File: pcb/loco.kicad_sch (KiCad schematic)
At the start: 121 parts, among them J1 I2C, J10 Stepper1, J11 Motor2, J12 PWR1, J13 PWR2, J14 Stepper1, J15 Stepper1, J2 EXT, J3 GPIO, J6 USB_C_Receptacle_USB2.0, J7 UART, J8 TagConnect, J9 Motor1, U1 LD1117S33TR_SOT223, U2 STM32C031CxUx, U3 STSPIN240, U4 STSPIN220, U5 AP22652_3x, U6 AP22652_3x, U7 AP22652_3x, U8 STSPIN220, U9 STSPIN220

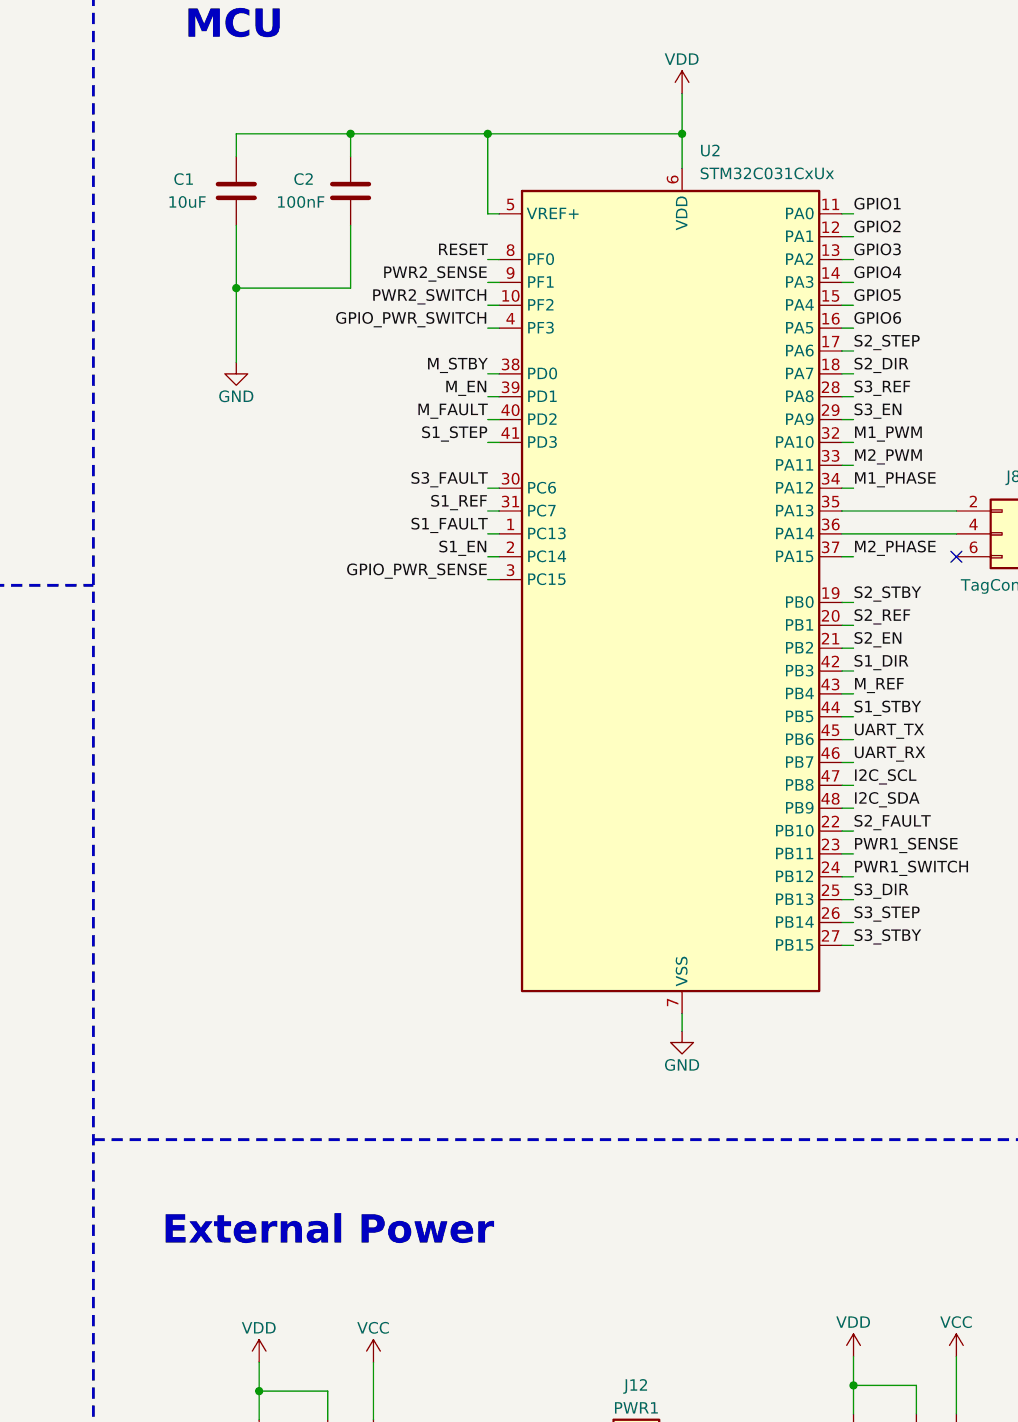
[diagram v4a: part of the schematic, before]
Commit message: add bom
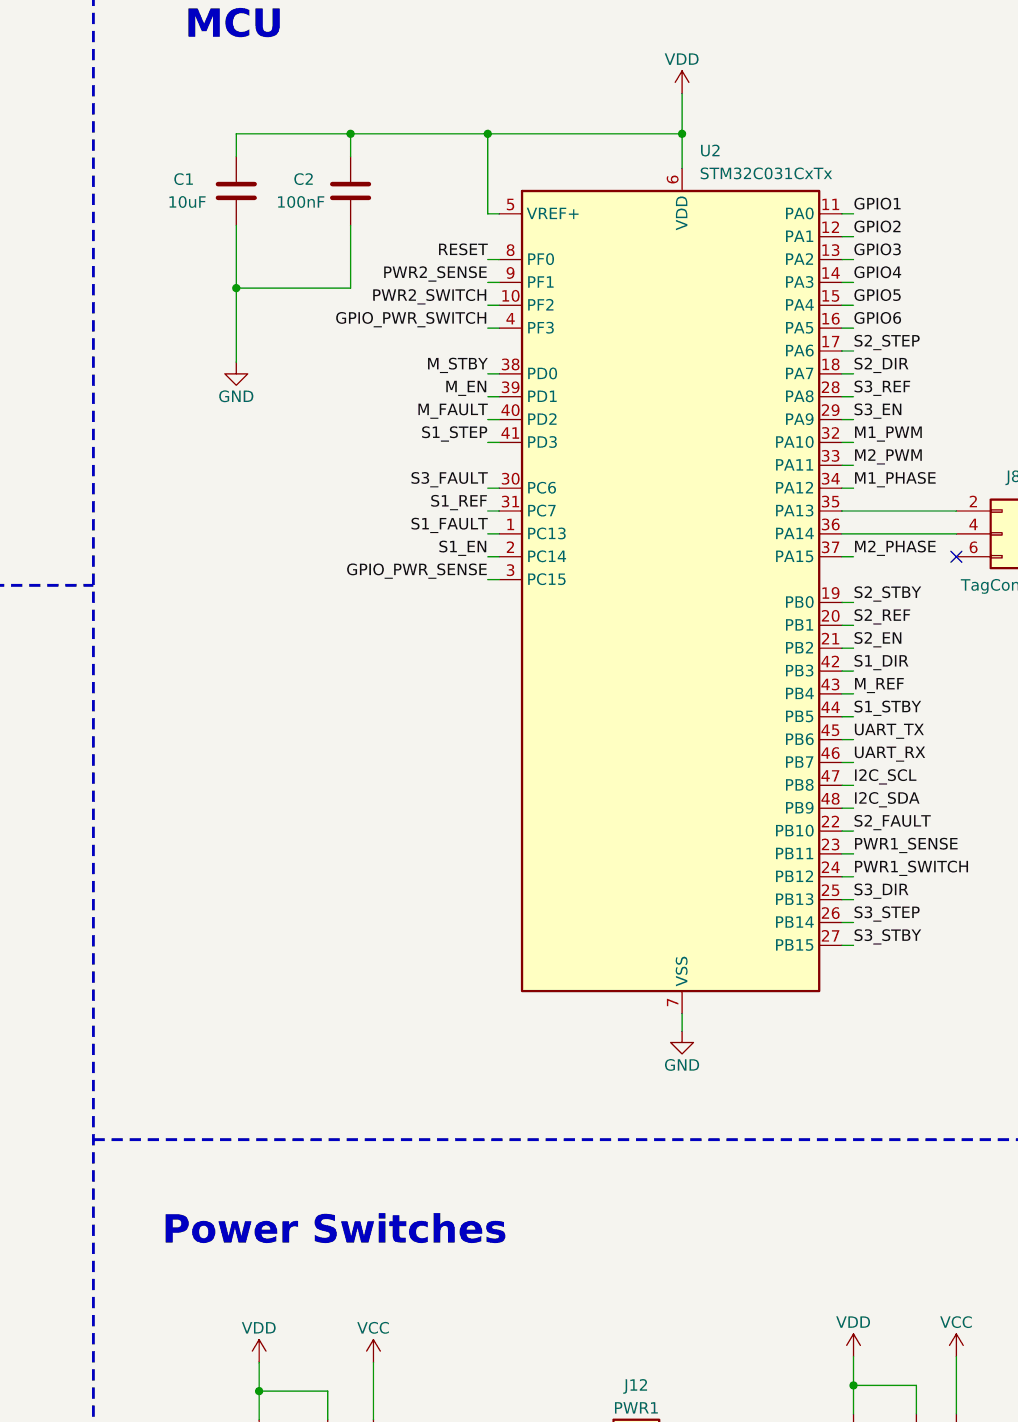
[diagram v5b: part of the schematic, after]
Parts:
- U2: value STM32C031CxUx -> STM32C031CxTx
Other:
- note added: "Power Switches"
- note removed: "External Power"
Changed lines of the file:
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@@
     (effects (font (size 3.14 3.14) (thickness 1) bold) (justify left bottom))
   )
-  (text "External Power" (at 280.035 159.385 0)
+  (text "Power Switches" (at 280.035 159.385 0)
     (effects (font (size 3.14 3.14) (thickness 1) bold) (justify left bottom))
   )
@@
       (effects (font (size 1.27 1.27)) (justify left))
     )
-    (property "Value" "STM32C031CxUx" (at 339.7759 40.005 0)
-      (effects (font (size 1.27 1.27)) (justify left))
-    )
+    (property "Value" "STM32C031CxTx" (at 339.7759 40.005 0)
+      (effects (font (size 1.27 1.27)) (justify left))
+    )
